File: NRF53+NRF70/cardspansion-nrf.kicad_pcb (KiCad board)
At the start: 2 copper layers, 22 x 30 mm, 4 parts, among them J1 M2-2230, U1 ME16WS03

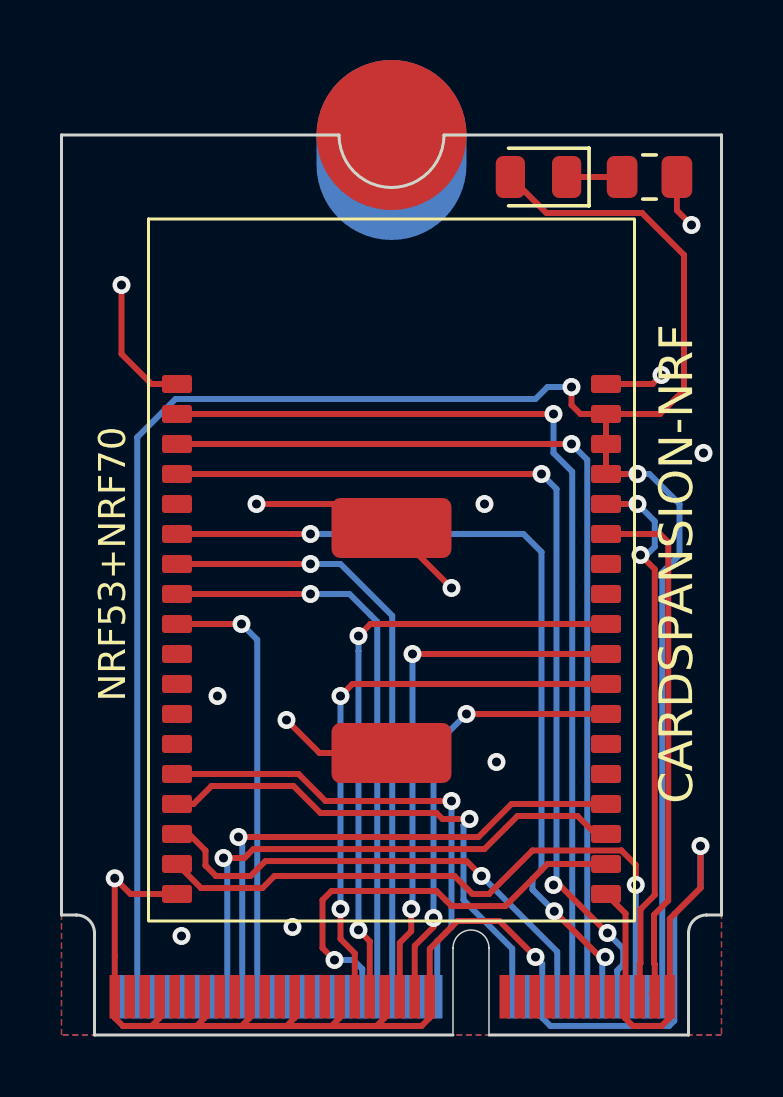
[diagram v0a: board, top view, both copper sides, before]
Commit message: Fix cardspansion-nrf I2S wiring
I2S-SDIN and I2S-SDOUT nets were switched around
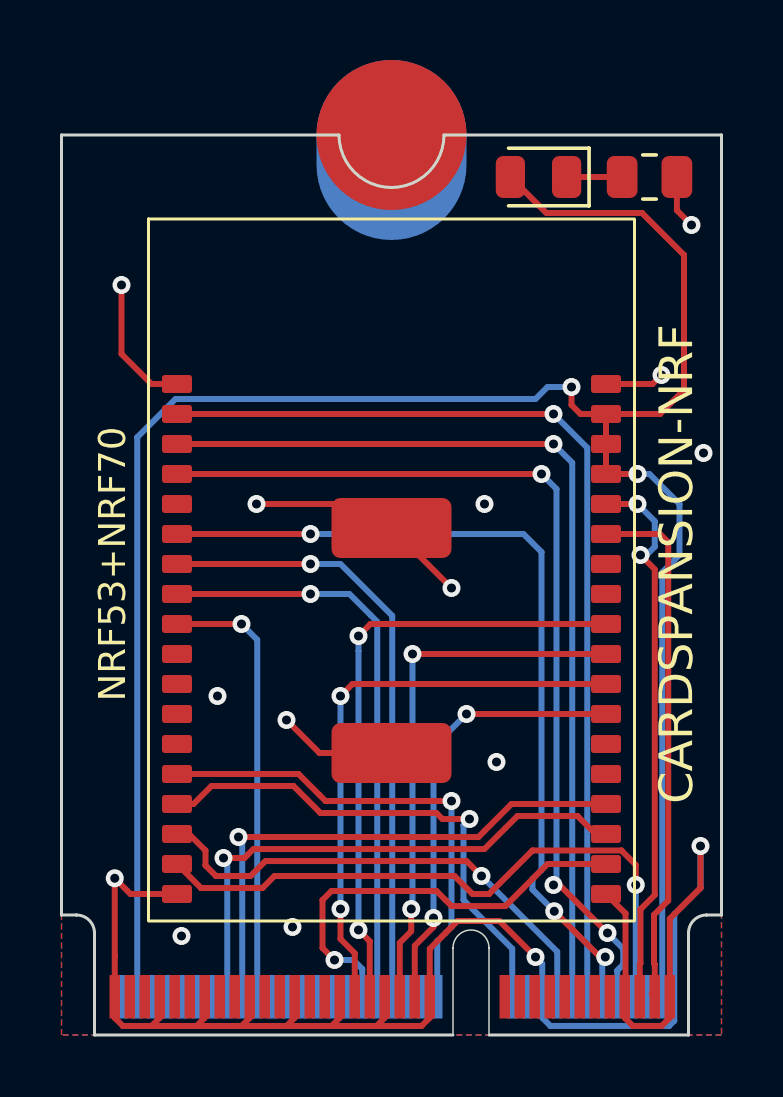
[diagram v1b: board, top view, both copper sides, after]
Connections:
- J1 pad 12: /I2S-SDOUT -> /I2S-SDIN
- J1 pad 14: /I2S-SDIN -> /I2S-SDOUT
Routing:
- net /I2S-SDOUT: track 31.8 -> 31.2 mm
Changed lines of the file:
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@@
 			(size 0.35 1.45)
 			(layers "B.Cu" "B.Mask")
-			(net 20 "/I2S-SDOUT")
+			(net 19 "/I2S-SDIN")
 			(pinfunction "PCM_IN/I2S_SD_IN")
 			(pintype "input")
@@
 			(size 0.35 1.45)
 			(layers "B.Cu" "B.Mask")
-			(net 19 "/I2S-SDIN")
+			(net 20 "/I2S-SDOUT")
 			(pinfunction "PCM_OUT/I2S_SD_OUT")
 			(pintype "output")
@@
 	)
 	(segment
-		(start 128.025 122.225)
+		(start 127.4 120.3)
+		(end 128.525 121.425)
+		(width 0.2)
+		(layer "B.Cu")
+		(net 19)
+	)
+	(segment
+		(start 128.525 121.425)
+		(end 128.525 139.725)
+		(width 0.2)
+		(layer "B.Cu")
+		(net 19)
+	)
+	(segment
+		(start 114.85 121.3)
+		(end 127.4 121.3)
+		(width 0.2)
+		(layer "F.Cu")
+		(net 20)
+	)
+	(via
+		(at 127.4 121.3)
+		(size 0.6)
+		(drill 0.3)
+		(layers "F.Cu" "B.Cu")
+		(net 20)
+	)
+	(segment
+		(start 127.4 121.3)
+		(end 128.025 121.925)
+		(width 0.2)
+		(layer "B.Cu")
+		(net 20)
+	)
+	(segment
+		(start 128.025 121.925)
 		(end 128.025 139.725)
 		(width 0.2)
 		(layer "B.Cu")
-		(net 19)
-	)
-	(segment
-		(start 127.4 120.3)
-		(end 127.4 121.6)
-		(width 0.2)
-		(layer "B.Cu")
-		(net 19)
-	)
-	(segment
-		(start 127.4 121.6)
-		(end 128.025 122.225)
-		(width 0.2)
-		(layer "B.Cu")
-		(net 19)
-	)
-	(segment
-		(start 114.85 121.3)
-		(end 128 121.3)
-		(width 0.2)
-		(layer "F.Cu")
-		(net 20)
-	)
-	(via
-		(at 128 121.3)
-		(size 0.6)
-		(drill 0.3)
-		(layers "F.Cu" "B.Cu")
-		(net 20)
-	)
-	(segment
-		(start 128 121.3)
-		(end 128.525 121.825)
-		(width 0.2)
-		(layer "B.Cu")
-		(net 20)
-	)
-	(segment
-		(start 128.525 121.825)
-		(end 128.525 139.725)
-		(width 0.2)
-		(layer "B.Cu")
